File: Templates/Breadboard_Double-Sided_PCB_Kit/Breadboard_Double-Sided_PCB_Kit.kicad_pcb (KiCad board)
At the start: 2 copper layers, 70 x 30 mm, 276 parts

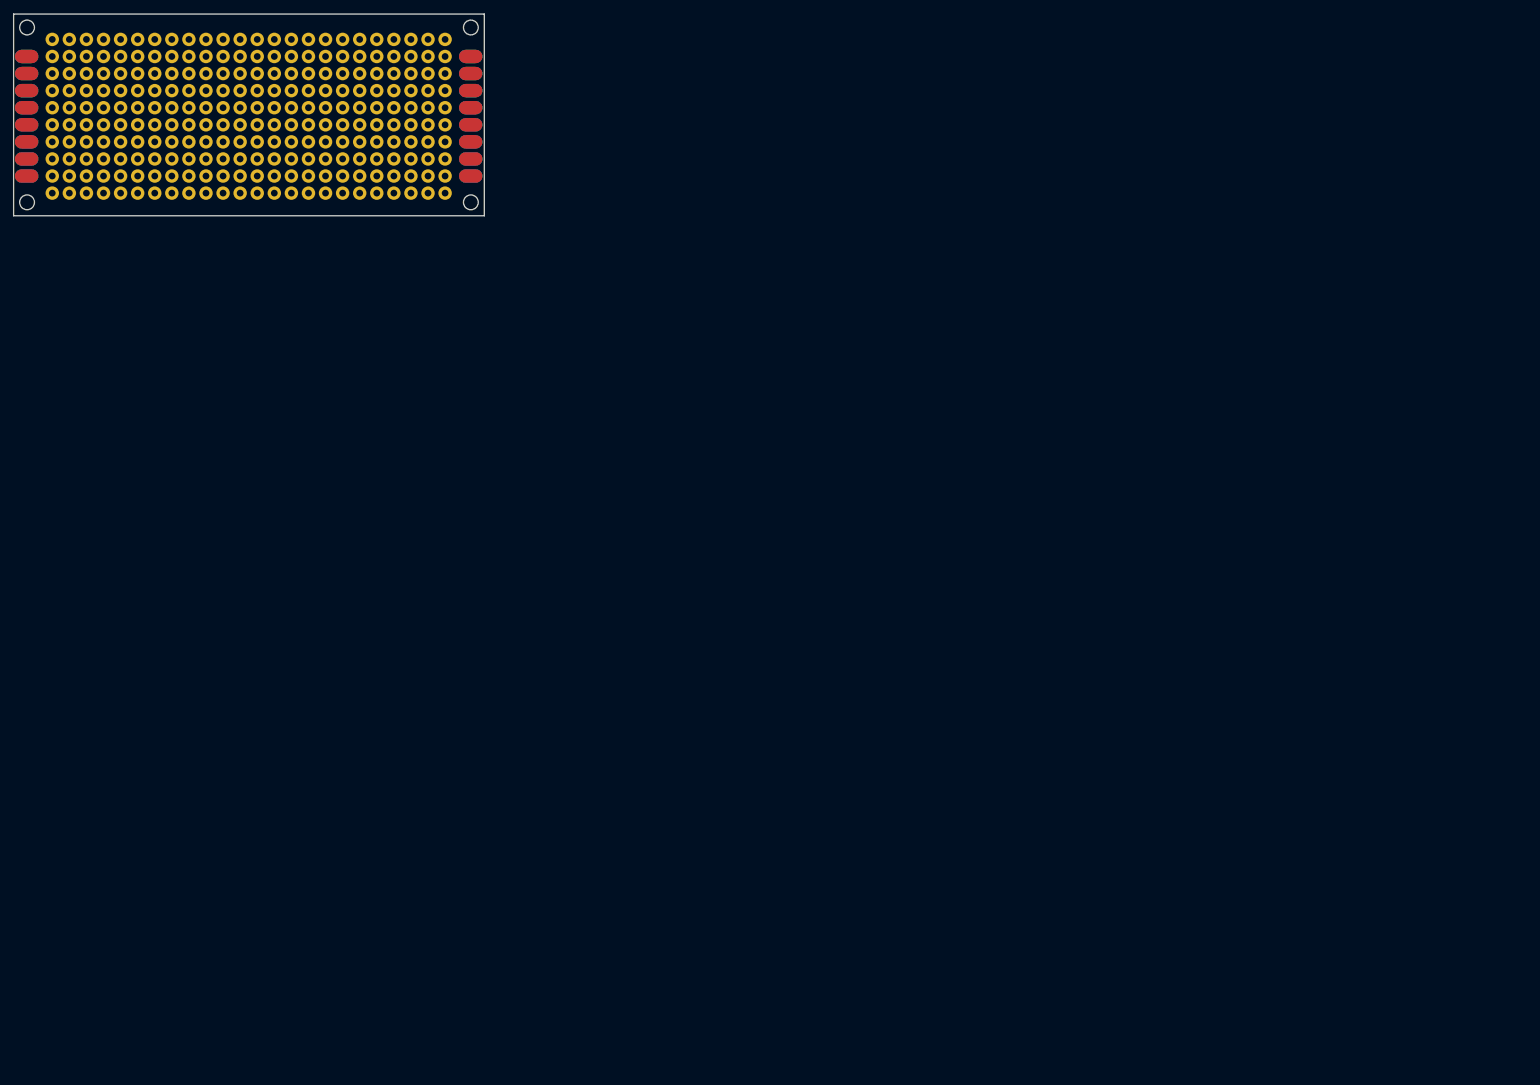
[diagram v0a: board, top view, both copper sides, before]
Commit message: Add all boards in PCB kit.
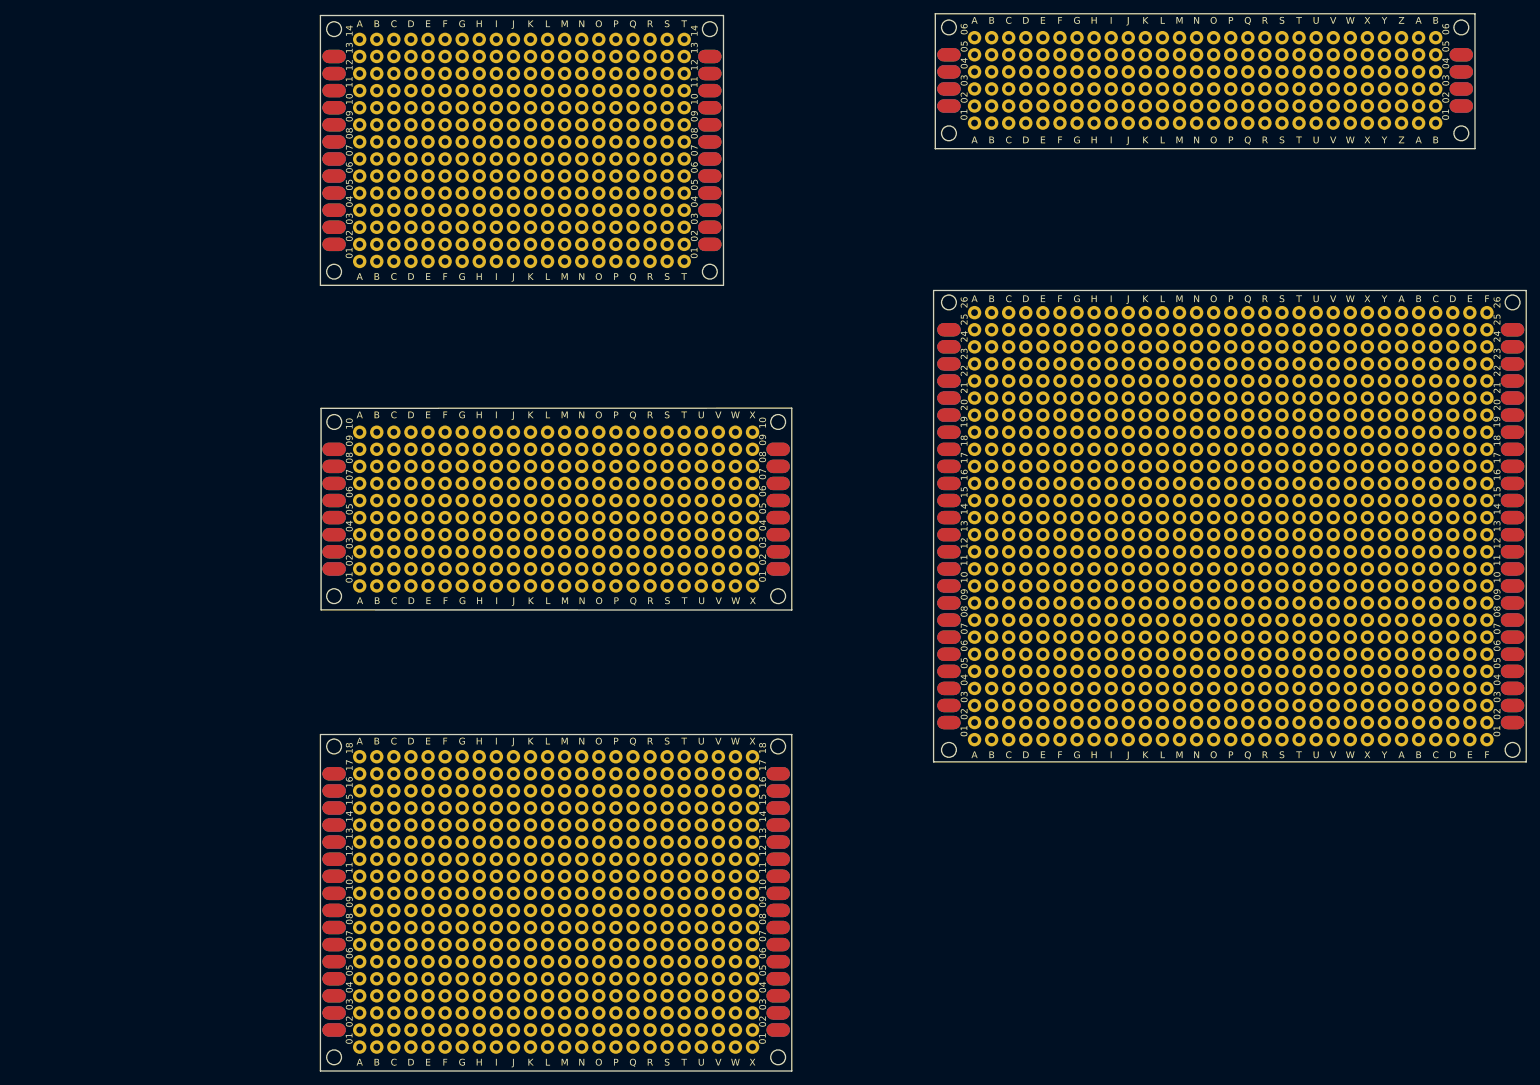
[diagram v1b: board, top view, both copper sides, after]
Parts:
- added REF**: Label, WallLabs:Breadboard_2.54mm_Pad_3.5x2mm, F.Cu at (245.1, 114.3)
- added REF**: Label, WallLabs:Breadboard_2.54mm_Pad_3.5x2mm, B.Cu at (245.1, 116.8)
- added REF**: Label, WallLabs:Breadboard_2.54mm_TH_Pad_2mm, F.Cu at (238.8, 132.1)
- added REF**: Label, WallLabs:Breadboard_2.54mm_TH_Pad_2mm, F.Cu at (104.1, 53.3)
- added REF**: Label, WallLabs:Breadboard_2.54mm_TH_Pad_2mm, F.Cu at (101.6, 53.3)
- added REF**: Label, WallLabs:Breadboard_2.54mm_TH_Pad_2mm, F.Cu at (99.1, 53.3)
- added REF**: Label, WallLabs:Breadboard_2.54mm_TH_Pad_2mm, F.Cu at (96.5, 53.3)
- added REF**: Label, WallLabs:Breadboard_2.54mm_TH_Pad_2mm, F.Cu at (94.0, 53.3)
- added REF**: Label, WallLabs:Breadboard_2.54mm_TH_Pad_2mm, F.Cu at (91.4, 53.3)
- added REF**: Label, WallLabs:Breadboard_2.54mm_TH_Pad_2mm, F.Cu at (88.9, 53.3)
- added REF**: Label, WallLabs:Breadboard_2.54mm_TH_Pad_2mm, F.Cu at (86.4, 53.3)
- added REF**: Label, WallLabs:Breadboard_2.54mm_TH_Pad_2mm, F.Cu at (83.8, 53.3)
- added REF**: Label, WallLabs:Breadboard_2.54mm_TH_Pad_2mm, F.Cu at (81.3, 53.3)
- added REF**: Label, WallLabs:Breadboard_2.54mm_TH_Pad_2mm, F.Cu at (236.2, 132.1)
- added REF**: Label, WallLabs:Breadboard_2.54mm_TH_Pad_2mm, F.Cu at (78.7, 53.3)
- added REF**: Label, WallLabs:Breadboard_2.54mm_TH_Pad_2mm, F.Cu at (76.2, 53.3)
- added REF**: Label, WallLabs:Breadboard_2.54mm_TH_Pad_2mm, F.Cu at (73.7, 53.3)
- added REF**: Label, WallLabs:Breadboard_2.54mm_TH_Pad_2mm, F.Cu at (121.9, 50.8)
- added REF**: Label, WallLabs:Breadboard_2.54mm_TH_Pad_2mm, F.Cu at (119.4, 50.8)
- added REF**: Label, WallLabs:Breadboard_2.54mm_TH_Pad_2mm, F.Cu at (116.8, 50.8)
- added REF**: Label, WallLabs:Breadboard_2.54mm_TH_Pad_2mm, F.Cu at (114.3, 50.8)
- added REF**: Label, WallLabs:Breadboard_2.54mm_TH_Pad_2mm, F.Cu at (111.8, 50.8)
- added REF**: Label, WallLabs:Breadboard_2.54mm_TH_Pad_2mm, F.Cu at (109.2, 50.8)
- added REF**: Label, WallLabs:Breadboard_2.54mm_TH_Pad_2mm, F.Cu at (106.7, 50.8)
- added REF**: Label, WallLabs:Breadboard_2.54mm_TH_Pad_2mm, F.Cu at (233.7, 132.1)
- added REF**: Label, WallLabs:Breadboard_2.54mm_TH_Pad_2mm, F.Cu at (104.1, 50.8)
- added REF**: Label, WallLabs:Breadboard_2.54mm_TH_Pad_2mm, F.Cu at (101.6, 50.8)
- added REF**: Label, WallLabs:Breadboard_2.54mm_TH_Pad_2mm, F.Cu at (99.1, 50.8)
- added REF**: Label, WallLabs:Breadboard_2.54mm_TH_Pad_2mm, F.Cu at (96.5, 50.8)
- added REF**: Label, WallLabs:Breadboard_2.54mm_TH_Pad_2mm, F.Cu at (94.0, 50.8)
- added REF**: Label, WallLabs:Breadboard_2.54mm_TH_Pad_2mm, F.Cu at (91.4, 50.8)
- added REF**: Label, WallLabs:Breadboard_2.54mm_TH_Pad_2mm, F.Cu at (88.9, 50.8)
- added REF**: Label, WallLabs:Breadboard_2.54mm_TH_Pad_2mm, F.Cu at (86.4, 50.8)
- added REF**: Label, WallLabs:Breadboard_2.54mm_TH_Pad_2mm, F.Cu at (83.8, 50.8)
- added REF**: Label, WallLabs:Breadboard_2.54mm_TH_Pad_2mm, F.Cu at (81.3, 50.8)
- added REF**: Label, WallLabs:Breadboard_2.54mm_TH_Pad_2mm, F.Cu at (231.1, 132.1)
- added REF**: Label, WallLabs:Breadboard_2.54mm_TH_Pad_2mm, F.Cu at (78.7, 50.8)
- added REF**: Label, WallLabs:Breadboard_2.54mm_TH_Pad_2mm, F.Cu at (76.2, 50.8)
- added REF**: Label, WallLabs:Breadboard_2.54mm_TH_Pad_2mm, F.Cu at (73.7, 50.8)
- added REF**: Label, WallLabs:Breadboard_2.54mm_TH_Pad_2mm, F.Cu at (121.9, 48.3)
- added REF**: Label, WallLabs:Breadboard_2.54mm_TH_Pad_2mm, F.Cu at (119.4, 48.3)
- added REF**: Label, WallLabs:Breadboard_2.54mm_TH_Pad_2mm, F.Cu at (116.8, 48.3)
- added REF**: Label, WallLabs:Breadboard_2.54mm_TH_Pad_2mm, F.Cu at (114.3, 48.3)
- added REF**: Label, WallLabs:Breadboard_2.54mm_TH_Pad_2mm, F.Cu at (111.8, 48.3)
- added REF**: Label, WallLabs:Breadboard_2.54mm_TH_Pad_2mm, F.Cu at (109.2, 48.3)
- added REF**: Label, WallLabs:Breadboard_2.54mm_TH_Pad_2mm, F.Cu at (106.7, 48.3)
- added REF**: Label, WallLabs:Breadboard_2.54mm_TH_Pad_2mm, F.Cu at (228.6, 132.1)
- added REF**: Label, WallLabs:Breadboard_2.54mm_TH_Pad_2mm, F.Cu at (104.1, 48.3)
- added REF**: Label, WallLabs:Breadboard_2.54mm_TH_Pad_2mm, F.Cu at (101.6, 48.3)
- added REF**: Label, WallLabs:Breadboard_2.54mm_TH_Pad_2mm, F.Cu at (99.1, 48.3)
- added REF**: Label, WallLabs:Breadboard_2.54mm_TH_Pad_2mm, F.Cu at (96.5, 48.3)
- added REF**: Label, WallLabs:Breadboard_2.54mm_TH_Pad_2mm, F.Cu at (94.0, 48.3)
- added REF**: Label, WallLabs:Breadboard_2.54mm_TH_Pad_2mm, F.Cu at (91.4, 48.3)
- added REF**: Label, WallLabs:Breadboard_2.54mm_TH_Pad_2mm, F.Cu at (88.9, 48.3)
- added REF**: Label, WallLabs:Breadboard_2.54mm_TH_Pad_2mm, F.Cu at (86.4, 48.3)
- added REF**: Label, WallLabs:Breadboard_2.54mm_TH_Pad_2mm, F.Cu at (83.8, 48.3)
- added REF**: Label, WallLabs:Breadboard_2.54mm_TH_Pad_2mm, F.Cu at (81.3, 48.3)
- added REF**: Label, WallLabs:Breadboard_2.54mm_TH_Pad_2mm, F.Cu at (226.1, 132.1)
- added REF**: Label, WallLabs:Breadboard_2.54mm_TH_Pad_2mm, F.Cu at (78.7, 48.3)
- added REF**: Label, WallLabs:Breadboard_2.54mm_TH_Pad_2mm, F.Cu at (76.2, 48.3)
- added REF**: Label, WallLabs:Breadboard_2.54mm_TH_Pad_2mm, F.Cu at (73.7, 48.3)
- added REF**: Label, WallLabs:Breadboard_2.54mm_TH_Pad_2mm, F.Cu at (121.9, 45.7)
- added REF**: Label, WallLabs:Breadboard_2.54mm_TH_Pad_2mm, F.Cu at (119.4, 45.7)
- added REF**: Label, WallLabs:Breadboard_2.54mm_TH_Pad_2mm, F.Cu at (116.8, 45.7)
- added REF**: Label, WallLabs:Breadboard_2.54mm_TH_Pad_2mm, F.Cu at (114.3, 45.7)
- added REF**: Label, WallLabs:Breadboard_2.54mm_TH_Pad_2mm, F.Cu at (111.8, 45.7)
- added REF**: Label, WallLabs:Breadboard_2.54mm_TH_Pad_2mm, F.Cu at (109.2, 45.7)
- added REF**: Label, WallLabs:Breadboard_2.54mm_TH_Pad_2mm, F.Cu at (106.7, 45.7)
- added REF**: Label, WallLabs:Breadboard_2.54mm_TH_Pad_2mm, F.Cu at (223.5, 132.1)
- added REF**: Label, WallLabs:Breadboard_2.54mm_TH_Pad_2mm, F.Cu at (104.1, 45.7)
- added REF**: Label, WallLabs:Breadboard_2.54mm_TH_Pad_2mm, F.Cu at (101.6, 45.7)
- added REF**: Label, WallLabs:Breadboard_2.54mm_TH_Pad_2mm, F.Cu at (99.1, 45.7)
- added REF**: Label, WallLabs:Breadboard_2.54mm_TH_Pad_2mm, F.Cu at (96.5, 45.7)
- added REF**: Label, WallLabs:Breadboard_2.54mm_TH_Pad_2mm, F.Cu at (94.0, 45.7)
- added REF**: Label, WallLabs:Breadboard_2.54mm_TH_Pad_2mm, F.Cu at (91.4, 45.7)
- added REF**: Label, WallLabs:Breadboard_2.54mm_TH_Pad_2mm, F.Cu at (88.9, 45.7)
- added REF**: Label, WallLabs:Breadboard_2.54mm_TH_Pad_2mm, F.Cu at (86.4, 45.7)
- added REF**: Label, WallLabs:Breadboard_2.54mm_TH_Pad_2mm, F.Cu at (83.8, 45.7)
- added REF**: Label, WallLabs:Breadboard_2.54mm_TH_Pad_2mm, F.Cu at (81.3, 45.7)
- added REF**: Label, WallLabs:Breadboard_2.54mm_TH_Pad_2mm, F.Cu at (221.0, 132.1)
- added REF**: Label, WallLabs:Breadboard_2.54mm_TH_Pad_2mm, F.Cu at (78.7, 45.7)
- added REF**: Label, WallLabs:Breadboard_2.54mm_TH_Pad_2mm, F.Cu at (76.2, 45.7)
- added REF**: Label, WallLabs:Breadboard_2.54mm_TH_Pad_2mm, F.Cu at (73.7, 45.7)
- added REF**: Label, WallLabs:Breadboard_2.54mm_TH_Pad_2mm, F.Cu at (121.9, 43.2)
- added REF**: Label, WallLabs:Breadboard_2.54mm_TH_Pad_2mm, F.Cu at (119.4, 43.2)
- added REF**: Label, WallLabs:Breadboard_2.54mm_TH_Pad_2mm, F.Cu at (116.8, 43.2)
- added REF**: Label, WallLabs:Breadboard_2.54mm_TH_Pad_2mm, F.Cu at (114.3, 43.2)
- added REF**: Label, WallLabs:Breadboard_2.54mm_TH_Pad_2mm, F.Cu at (111.8, 43.2)
- added REF**: Label, WallLabs:Breadboard_2.54mm_TH_Pad_2mm, F.Cu at (109.2, 43.2)
- added REF**: Label, WallLabs:Breadboard_2.54mm_TH_Pad_2mm, F.Cu at (106.7, 43.2)
- added REF**: Label, WallLabs:Breadboard_2.54mm_TH_Pad_2mm, F.Cu at (218.4, 132.1)
- added REF**: Label, WallLabs:Breadboard_2.54mm_TH_Pad_2mm, F.Cu at (104.1, 43.2)
- added REF**: Label, WallLabs:Breadboard_2.54mm_TH_Pad_2mm, F.Cu at (101.6, 43.2)
- added REF**: Label, WallLabs:Breadboard_2.54mm_TH_Pad_2mm, F.Cu at (99.1, 43.2)
- added REF**: Label, WallLabs:Breadboard_2.54mm_TH_Pad_2mm, F.Cu at (96.5, 43.2)
- added REF**: Label, WallLabs:Breadboard_2.54mm_TH_Pad_2mm, F.Cu at (94.0, 43.2)
- added REF**: Label, WallLabs:Breadboard_2.54mm_TH_Pad_2mm, F.Cu at (91.4, 43.2)
- added REF**: Label, WallLabs:Breadboard_2.54mm_TH_Pad_2mm, F.Cu at (88.9, 43.2)
- added REF**: Label, WallLabs:Breadboard_2.54mm_TH_Pad_2mm, F.Cu at (86.4, 43.2)
- added REF**: Label, WallLabs:Breadboard_2.54mm_TH_Pad_2mm, F.Cu at (83.8, 43.2)
- added REF**: Label, WallLabs:Breadboard_2.54mm_TH_Pad_2mm, F.Cu at (81.3, 43.2)
- added REF**: Label, WallLabs:Breadboard_2.54mm_TH_Pad_2mm, F.Cu at (215.9, 132.1)
- added REF**: Label, WallLabs:Breadboard_2.54mm_TH_Pad_2mm, F.Cu at (78.7, 43.2)
- added REF**: Label, WallLabs:Breadboard_2.54mm_TH_Pad_2mm, F.Cu at (76.2, 43.2)
- added REF**: Label, WallLabs:Breadboard_2.54mm_TH_Pad_2mm, F.Cu at (73.7, 43.2)
- added REF**: Label, WallLabs:Breadboard_2.54mm_TH_Pad_2mm, F.Cu at (121.9, 40.6)
- added REF**: Label, WallLabs:Breadboard_2.54mm_TH_Pad_2mm, F.Cu at (119.4, 40.6)
- added REF**: Label, WallLabs:Breadboard_2.54mm_TH_Pad_2mm, F.Cu at (116.8, 40.6)
- added REF**: Label, WallLabs:Breadboard_2.54mm_TH_Pad_2mm, F.Cu at (114.3, 40.6)
- added REF**: Label, WallLabs:Breadboard_2.54mm_TH_Pad_2mm, F.Cu at (111.8, 40.6)
- added REF**: Label, WallLabs:Breadboard_2.54mm_TH_Pad_2mm, F.Cu at (109.2, 40.6)
- added REF**: Label, WallLabs:Breadboard_2.54mm_TH_Pad_2mm, F.Cu at (106.7, 40.6)
- added REF**: Label, WallLabs:Breadboard_2.54mm_Pad_3.5x2mm, F.Cu at (245.1, 104.1)
- added REF**: Label, WallLabs:Breadboard_2.54mm_TH_Pad_2mm, F.Cu at (213.4, 132.1)
- added REF**: Label, WallLabs:Breadboard_2.54mm_TH_Pad_2mm, F.Cu at (104.1, 40.6)
- added REF**: Label, WallLabs:Breadboard_2.54mm_TH_Pad_2mm, F.Cu at (101.6, 40.6)
- added REF**: Label, WallLabs:Breadboard_2.54mm_TH_Pad_2mm, F.Cu at (99.1, 40.6)
- added REF**: Label, WallLabs:Breadboard_2.54mm_TH_Pad_2mm, F.Cu at (96.5, 40.6)
- added REF**: Label, WallLabs:Breadboard_2.54mm_TH_Pad_2mm, F.Cu at (94.0, 40.6)
- added REF**: Label, WallLabs:Breadboard_2.54mm_TH_Pad_2mm, F.Cu at (91.4, 40.6)
- added REF**: Label, WallLabs:Breadboard_2.54mm_TH_Pad_2mm, F.Cu at (88.9, 40.6)
- added REF**: Label, WallLabs:Breadboard_2.54mm_TH_Pad_2mm, F.Cu at (86.4, 40.6)
- added REF**: Label, WallLabs:Breadboard_2.54mm_TH_Pad_2mm, F.Cu at (83.8, 40.6)
- added REF**: Label, WallLabs:Breadboard_2.54mm_TH_Pad_2mm, F.Cu at (81.3, 40.6)
- added REF**: Label, WallLabs:Breadboard_2.54mm_TH_Pad_2mm, F.Cu at (210.8, 132.1)
- added REF**: Label, WallLabs:Breadboard_2.54mm_TH_Pad_2mm, F.Cu at (78.7, 40.6)
- added REF**: Label, WallLabs:Breadboard_2.54mm_TH_Pad_2mm, F.Cu at (76.2, 40.6)
- added REF**: Label, WallLabs:Breadboard_2.54mm_TH_Pad_2mm, F.Cu at (73.7, 40.6)
- added REF**: Label, WallLabs:Breadboard_2.54mm_TH_Pad_2mm, F.Cu at (121.9, 38.1)
- added REF**: Label, WallLabs:Breadboard_2.54mm_TH_Pad_2mm, F.Cu at (119.4, 38.1)
- added REF**: Label, WallLabs:Breadboard_2.54mm_TH_Pad_2mm, F.Cu at (116.8, 38.1)
- added REF**: Label, WallLabs:Breadboard_2.54mm_TH_Pad_2mm, F.Cu at (114.3, 38.1)
- added REF**: Label, WallLabs:Breadboard_2.54mm_TH_Pad_2mm, F.Cu at (111.8, 38.1)
- added REF**: Label, WallLabs:Breadboard_2.54mm_TH_Pad_2mm, F.Cu at (109.2, 38.1)
- added REF**: Label, WallLabs:Breadboard_2.54mm_TH_Pad_2mm, F.Cu at (106.7, 38.1)
- added REF**: Label, WallLabs:Breadboard_2.54mm_TH_Pad_2mm, F.Cu at (208.3, 132.1)
- added REF**: Label, WallLabs:Breadboard_2.54mm_TH_Pad_2mm, F.Cu at (104.1, 38.1)
- added REF**: Label, WallLabs:Breadboard_2.54mm_TH_Pad_2mm, F.Cu at (101.6, 38.1)
- added REF**: Label, WallLabs:Breadboard_2.54mm_TH_Pad_2mm, F.Cu at (99.1, 38.1)
- added REF**: Label, WallLabs:Breadboard_2.54mm_TH_Pad_2mm, F.Cu at (96.5, 38.1)
- added REF**: Label, WallLabs:Breadboard_2.54mm_TH_Pad_2mm, F.Cu at (94.0, 38.1)
- added REF**: Label, WallLabs:Breadboard_2.54mm_TH_Pad_2mm, F.Cu at (91.4, 38.1)
- added REF**: Label, WallLabs:Breadboard_2.54mm_TH_Pad_2mm, F.Cu at (88.9, 38.1)
- added REF**: Label, WallLabs:Breadboard_2.54mm_TH_Pad_2mm, F.Cu at (86.4, 38.1)
- added REF**: Label, WallLabs:Breadboard_2.54mm_TH_Pad_2mm, F.Cu at (83.8, 38.1)
- added REF**: Label, WallLabs:Breadboard_2.54mm_TH_Pad_2mm, F.Cu at (81.3, 38.1)
- added REF**: Label, WallLabs:Breadboard_2.54mm_TH_Pad_2mm, F.Cu at (205.7, 132.1)
- added REF**: Label, WallLabs:Breadboard_2.54mm_TH_Pad_2mm, F.Cu at (78.7, 38.1)
- added REF**: Label, WallLabs:Breadboard_2.54mm_TH_Pad_2mm, F.Cu at (76.2, 38.1)
- added REF**: Label, WallLabs:Breadboard_2.54mm_TH_Pad_2mm, F.Cu at (73.7, 38.1)
- added REF**: Label, WallLabs:Breadboard_2.54mm_TH_Pad_2mm, F.Cu at (121.9, 35.6)
- added REF**: Label, WallLabs:Breadboard_2.54mm_TH_Pad_2mm, F.Cu at (119.4, 35.6)
- added REF**: Label, WallLabs:Breadboard_2.54mm_TH_Pad_2mm, F.Cu at (116.8, 35.6)
- added REF**: Label, WallLabs:Breadboard_2.54mm_TH_Pad_2mm, F.Cu at (114.3, 35.6)
- added REF**: Label, WallLabs:Breadboard_2.54mm_TH_Pad_2mm, F.Cu at (111.8, 35.6)
- added REF**: Label, WallLabs:Breadboard_2.54mm_TH_Pad_2mm, F.Cu at (109.2, 35.6)
- added REF**: Label, WallLabs:Breadboard_2.54mm_TH_Pad_2mm, F.Cu at (106.7, 35.6)
- added REF**: Label, WallLabs:Breadboard_2.54mm_TH_Pad_2mm, F.Cu at (203.2, 132.1)
- added REF**: Label, WallLabs:Breadboard_2.54mm_TH_Pad_2mm, F.Cu at (104.1, 35.6)
- added REF**: Label, WallLabs:Breadboard_2.54mm_TH_Pad_2mm, F.Cu at (101.6, 35.6)
- added REF**: Label, WallLabs:Breadboard_2.54mm_TH_Pad_2mm, F.Cu at (99.1, 35.6)
- added REF**: Label, WallLabs:Breadboard_2.54mm_TH_Pad_2mm, F.Cu at (96.5, 35.6)
- added REF**: Label, WallLabs:Breadboard_2.54mm_TH_Pad_2mm, F.Cu at (94.0, 35.6)
- added REF**: Label, WallLabs:Breadboard_2.54mm_TH_Pad_2mm, F.Cu at (91.4, 35.6)
- added REF**: Label, WallLabs:Breadboard_2.54mm_TH_Pad_2mm, F.Cu at (88.9, 35.6)
- added REF**: Label, WallLabs:Breadboard_2.54mm_TH_Pad_2mm, F.Cu at (86.4, 35.6)
- added REF**: Label, WallLabs:Breadboard_2.54mm_TH_Pad_2mm, F.Cu at (83.8, 35.6)
- added REF**: Label, WallLabs:Breadboard_2.54mm_TH_Pad_2mm, F.Cu at (81.3, 35.6)
- added REF**: Label, WallLabs:Breadboard_2.54mm_TH_Pad_2mm, F.Cu at (200.7, 132.1)
- added REF**: Label, WallLabs:Breadboard_2.54mm_TH_Pad_2mm, F.Cu at (78.7, 35.6)
- added REF**: Label, WallLabs:Breadboard_2.54mm_TH_Pad_2mm, F.Cu at (76.2, 35.6)
- added REF**: Label, WallLabs:Breadboard_2.54mm_TH_Pad_2mm, F.Cu at (73.7, 35.6)
- added REF**: Label, WallLabs:Breadboard_2.54mm_TH_Pad_2mm, F.Cu at (121.9, 33.0)
- added REF**: Label, WallLabs:Breadboard_2.54mm_TH_Pad_2mm, F.Cu at (119.4, 33.0)
- added REF**: Label, WallLabs:Breadboard_2.54mm_TH_Pad_2mm, F.Cu at (116.8, 33.0)
- added REF**: Label, WallLabs:Breadboard_2.54mm_TH_Pad_2mm, F.Cu at (114.3, 33.0)
- added REF**: Label, WallLabs:Breadboard_2.54mm_TH_Pad_2mm, F.Cu at (111.8, 33.0)
- added REF**: Label, WallLabs:Breadboard_2.54mm_TH_Pad_2mm, F.Cu at (109.2, 33.0)
- added REF**: Label, WallLabs:Breadboard_2.54mm_TH_Pad_2mm, F.Cu at (106.7, 33.0)
- added REF**: Label, WallLabs:Breadboard_2.54mm_TH_Pad_2mm, F.Cu at (198.1, 132.1)
- added REF**: Label, WallLabs:Breadboard_2.54mm_TH_Pad_2mm, F.Cu at (104.1, 33.0)
- added REF**: Label, WallLabs:Breadboard_2.54mm_TH_Pad_2mm, F.Cu at (101.6, 33.0)
- added REF**: Label, WallLabs:Breadboard_2.54mm_TH_Pad_2mm, F.Cu at (99.1, 33.0)
- added REF**: Label, WallLabs:Breadboard_2.54mm_TH_Pad_2mm, F.Cu at (96.5, 33.0)
- added REF**: Label, WallLabs:Breadboard_2.54mm_TH_Pad_2mm, F.Cu at (94.0, 33.0)
- added REF**: Label, WallLabs:Breadboard_2.54mm_TH_Pad_2mm, F.Cu at (91.4, 33.0)
- added REF**: Label, WallLabs:Breadboard_2.54mm_TH_Pad_2mm, F.Cu at (88.9, 33.0)
- added REF**: Label, WallLabs:Breadboard_2.54mm_TH_Pad_2mm, F.Cu at (86.4, 33.0)
- added REF**: Label, WallLabs:Breadboard_2.54mm_TH_Pad_2mm, F.Cu at (83.8, 33.0)
- added REF**: Label, WallLabs:Breadboard_2.54mm_TH_Pad_2mm, F.Cu at (81.3, 33.0)
- added REF**: Label, WallLabs:Breadboard_2.54mm_TH_Pad_2mm, F.Cu at (195.6, 132.1)
- added REF**: Label, WallLabs:Breadboard_2.54mm_TH_Pad_2mm, F.Cu at (78.7, 33.0)
- added REF**: Label, WallLabs:Breadboard_2.54mm_TH_Pad_2mm, F.Cu at (76.2, 33.0)
- added REF**: Label, WallLabs:Breadboard_2.54mm_TH_Pad_2mm, F.Cu at (73.7, 33.0)
- added REF**: Label, WallLabs:Breadboard_2.54mm_TH_Pad_2mm, F.Cu at (121.9, 30.5)
- added REF**: Label, WallLabs:Breadboard_2.54mm_TH_Pad_2mm, F.Cu at (119.4, 30.5)
- added REF**: Label, WallLabs:Breadboard_2.54mm_TH_Pad_2mm, F.Cu at (116.8, 30.5)
- added REF**: Label, WallLabs:Breadboard_2.54mm_TH_Pad_2mm, F.Cu at (114.3, 30.5)
- added REF**: Label, WallLabs:Breadboard_2.54mm_TH_Pad_2mm, F.Cu at (111.8, 30.5)
- added REF**: Label, WallLabs:Breadboard_2.54mm_TH_Pad_2mm, F.Cu at (109.2, 30.5)
- added REF**: Label, WallLabs:Breadboard_2.54mm_TH_Pad_2mm, F.Cu at (106.7, 30.5)
- added REF**: Label, WallLabs:Breadboard_2.54mm_TH_Pad_2mm, F.Cu at (193.0, 132.1)
- added REF**: Label, WallLabs:Breadboard_2.54mm_TH_Pad_2mm, F.Cu at (104.1, 30.5)
- added REF**: Label, WallLabs:Breadboard_2.54mm_TH_Pad_2mm, F.Cu at (101.6, 30.5)
- added REF**: Label, WallLabs:Breadboard_2.54mm_TH_Pad_2mm, F.Cu at (99.1, 30.5)
- added REF**: Label, WallLabs:Breadboard_2.54mm_TH_Pad_2mm, F.Cu at (96.5, 30.5)
- added REF**: Label, WallLabs:Breadboard_2.54mm_TH_Pad_2mm, F.Cu at (94.0, 30.5)
- added REF**: Label, WallLabs:Breadboard_2.54mm_TH_Pad_2mm, F.Cu at (91.4, 30.5)
- added REF**: Label, WallLabs:Breadboard_2.54mm_TH_Pad_2mm, F.Cu at (88.9, 30.5)
- added REF**: Label, WallLabs:Breadboard_2.54mm_TH_Pad_2mm, F.Cu at (86.4, 30.5)
- added REF**: Label, WallLabs:Breadboard_2.54mm_TH_Pad_2mm, F.Cu at (83.8, 30.5)
- added REF**: Label, WallLabs:Breadboard_2.54mm_TH_Pad_2mm, F.Cu at (81.3, 30.5)
- added REF**: Label, WallLabs:Breadboard_2.54mm_TH_Pad_2mm, F.Cu at (190.5, 132.1)
- added REF**: Label, WallLabs:Breadboard_2.54mm_TH_Pad_2mm, F.Cu at (78.7, 30.5)
- added REF**: Label, WallLabs:Breadboard_2.54mm_TH_Pad_2mm, F.Cu at (76.2, 30.5)
- added REF**: Label, WallLabs:Breadboard_2.54mm_TH_Pad_2mm, F.Cu at (73.7, 30.5)
- added REF**: Label, WallLabs:Breadboard_2.54mm_TH_Pad_2mm, F.Cu at (121.9, 27.9)
- added REF**: Label, WallLabs:Breadboard_2.54mm_TH_Pad_2mm, F.Cu at (119.4, 27.9)
- added REF**: Label, WallLabs:Breadboard_2.54mm_TH_Pad_2mm, F.Cu at (116.8, 27.9)
- added REF**: Label, WallLabs:Breadboard_2.54mm_TH_Pad_2mm, F.Cu at (114.3, 27.9)
- added REF**: Label, WallLabs:Breadboard_2.54mm_TH_Pad_2mm, F.Cu at (111.8, 27.9)
- added REF**: Label, WallLabs:Breadboard_2.54mm_TH_Pad_2mm, F.Cu at (109.2, 27.9)
- added REF**: Label, WallLabs:Breadboard_2.54mm_TH_Pad_2mm, F.Cu at (106.7, 27.9)
- added REF**: Label, WallLabs:Breadboard_2.54mm_Pad_3.5x2mm, F.Cu at (245.1, 99.1)
- added REF**: Label, WallLabs:Breadboard_2.54mm_TH_Pad_2mm, F.Cu at (188.0, 132.1)
- added REF**: Label, WallLabs:Breadboard_2.54mm_TH_Pad_2mm, F.Cu at (104.1, 27.9)
- added REF**: Label, WallLabs:Breadboard_2.54mm_TH_Pad_2mm, F.Cu at (101.6, 27.9)
- added REF**: Label, WallLabs:Breadboard_2.54mm_TH_Pad_2mm, F.Cu at (99.1, 27.9)
- added REF**: Label, WallLabs:Breadboard_2.54mm_TH_Pad_2mm, F.Cu at (96.5, 27.9)
- added REF**: Label, WallLabs:Breadboard_2.54mm_TH_Pad_2mm, F.Cu at (94.0, 27.9)
- added REF**: Label, WallLabs:Breadboard_2.54mm_TH_Pad_2mm, F.Cu at (91.4, 27.9)
- added REF**: Label, WallLabs:Breadboard_2.54mm_TH_Pad_2mm, F.Cu at (88.9, 27.9)
- added REF**: Label, WallLabs:Breadboard_2.54mm_TH_Pad_2mm, F.Cu at (86.4, 27.9)
- added REF**: Label, WallLabs:Breadboard_2.54mm_TH_Pad_2mm, F.Cu at (83.8, 27.9)
- added REF**: Label, WallLabs:Breadboard_2.54mm_TH_Pad_2mm, F.Cu at (81.3, 27.9)
- added REF**: Label, WallLabs:Breadboard_2.54mm_TH_Pad_2mm, F.Cu at (185.4, 132.1)
- added REF**: Label, WallLabs:Breadboard_2.54mm_TH_Pad_2mm, F.Cu at (78.7, 27.9)
- added REF**: Label, WallLabs:Breadboard_2.54mm_TH_Pad_2mm, F.Cu at (76.2, 27.9)
- added REF**: Label, WallLabs:Breadboard_2.54mm_Pad_3.5x2mm, B.Cu at (69.8, 30.5)
- added REF**: Label, WallLabs:Breadboard_2.54mm_TH_Pad_2mm, F.Cu at (73.7, 27.9)
- added REF**: Label, WallLabs:Breadboard_2.54mm_Pad_3.5x2mm, F.Cu at (69.8, 30.5)
- added REF**: Label, WallLabs:Breadboard_2.54mm_Pad_3.5x2mm, F.Cu at (69.8, 58.4)
- added REF**: Label, WallLabs:Breadboard_2.54mm_Pad_3.5x2mm, B.Cu at (69.8, 58.4)
- added REF**: MountingHole_2.2mm_M2_ISO14580, MountingHole:MountingHole_2.2mm_M2_ISO14580, F.Cu at (69.8, 62.5)
- added REF**: Label, WallLabs:Breadboard_2.54mm_Pad_3.5x2mm, F.Cu at (69.8, 53.3)
- added REF**: Label, WallLabs:Breadboard_2.54mm_Pad_3.5x2mm, F.Cu at (69.8, 55.9)
- added REF**: Label, WallLabs:Breadboard_2.54mm_TH_Pad_2mm, F.Cu at (182.9, 132.1)
- added REF**: Label, WallLabs:Breadboard_2.54mm_Pad_3.5x2mm, B.Cu at (69.8, 55.9)
- added REF**: Label, WallLabs:Breadboard_2.54mm_Pad_3.5x2mm, B.Cu at (69.8, 53.3)
- added REF**: Label, WallLabs:Breadboard_2.54mm_Pad_3.5x2mm, F.Cu at (69.8, 50.8)
- added REF**: Label, WallLabs:Breadboard_2.54mm_Pad_3.5x2mm, B.Cu at (69.8, 50.8)
- added REF**: Label, WallLabs:Breadboard_2.54mm_Pad_3.5x2mm, F.Cu at (69.8, 48.3)
- added REF**: Label, WallLabs:Breadboard_2.54mm_Pad_3.5x2mm, B.Cu at (69.8, 35.6)
- added REF**: Label, WallLabs:Breadboard_2.54mm_Pad_3.5x2mm, F.Cu at (69.8, 43.2)
- added REF**: Label, WallLabs:Breadboard_2.54mm_Pad_3.5x2mm, B.Cu at (69.8, 38.1)
- added REF**: Label, WallLabs:Breadboard_2.54mm_Pad_3.5x2mm, F.Cu at (69.8, 45.7)
- added REF**: Label, WallLabs:Breadboard_2.54mm_Pad_3.5x2mm, B.Cu at (69.8, 40.6)
- added REF**: Label, WallLabs:Breadboard_2.54mm_TH_Pad_2mm, F.Cu at (180.3, 132.1)
- added REF**: Label, WallLabs:Breadboard_2.54mm_Pad_3.5x2mm, F.Cu at (69.8, 35.6)
- added REF**: Label, WallLabs:Breadboard_2.54mm_Pad_3.5x2mm, B.Cu at (69.8, 43.2)
- added REF**: Label, WallLabs:Breadboard_2.54mm_Pad_3.5x2mm, B.Cu at (69.8, 48.3)
- added REF**: Label, WallLabs:Breadboard_2.54mm_Pad_3.5x2mm, B.Cu at (69.8, 33.0)
- added REF**: Label, WallLabs:Breadboard_2.54mm_Pad_3.5x2mm, F.Cu at (69.8, 38.1)
- added REF**: Label, WallLabs:Breadboard_2.54mm_Pad_3.5x2mm, F.Cu at (69.8, 33.0)
- added REF**: Label, WallLabs:Breadboard_2.54mm_Pad_3.5x2mm, B.Cu at (69.8, 45.7)
- added REF**: Label, WallLabs:Breadboard_2.54mm_Pad_3.5x2mm, F.Cu at (69.8, 40.6)
- added REF**: MountingHole_2.2mm_M2_ISO14580, MountingHole:MountingHole_2.2mm_M2_ISO14580, F.Cu at (69.8, 26.4)
- added REF**: Label, WallLabs:Breadboard_2.54mm_Pad_3.5x2mm, B.Cu at (135.9, 165.1)
- added REF**: Label, WallLabs:Breadboard_2.54mm_TH_Pad_2mm, F.Cu at (177.8, 132.1)
- added REF**: Label, WallLabs:Breadboard_2.54mm_Pad_3.5x2mm, B.Cu at (135.9, 157.5)
- added REF**: Label, WallLabs:Breadboard_2.54mm_Pad_3.5x2mm, B.Cu at (135.9, 167.6)
- added REF**: Label, WallLabs:Breadboard_2.54mm_Pad_3.5x2mm, B.Cu at (135.9, 154.9)
- added REF**: Label, WallLabs:Breadboard_2.54mm_Pad_3.5x2mm, B.Cu at (135.9, 160.0)
- added REF**: Label, WallLabs:Breadboard_2.54mm_Pad_3.5x2mm, B.Cu at (135.9, 152.4)
- added REF**: Label, WallLabs:Breadboard_2.54mm_Pad_3.5x2mm, B.Cu at (135.9, 170.2)
- added REF**: Label, WallLabs:Breadboard_2.54mm_Pad_3.5x2mm, B.Cu at (135.9, 175.3)
- added REF**: Label, WallLabs:Breadboard_2.54mm_Pad_3.5x2mm, B.Cu at (135.9, 142.2)
- added REF**: Label, WallLabs:Breadboard_2.54mm_Pad_3.5x2mm, B.Cu at (135.9, 147.3)
- added REF**: Label, WallLabs:Breadboard_2.54mm_Pad_3.5x2mm, B.Cu at (135.9, 162.6)
- added REF**: Label, WallLabs:Breadboard_2.54mm_TH_Pad_2mm, F.Cu at (175.3, 132.1)
- added REF**: Label, WallLabs:Breadboard_2.54mm_Pad_3.5x2mm, B.Cu at (135.9, 144.8)
- added REF**: Label, WallLabs:Breadboard_2.54mm_Pad_3.5x2mm, B.Cu at (135.9, 139.7)
- added REF**: Label, WallLabs:Breadboard_2.54mm_Pad_3.5x2mm, B.Cu at (135.9, 172.7)
- added REF**: Label, WallLabs:Breadboard_2.54mm_Pad_3.5x2mm, B.Cu at (135.9, 149.9)
- added REF**: Label, WallLabs:Breadboard_2.54mm_Pad_3.5x2mm, B.Cu at (135.9, 137.2)
- added REF**: Label, WallLabs:Breadboard_2.54mm_Pad_3.5x2mm, B.Cu at (69.8, 149.9)
- added REF**: Label, WallLabs:Breadboard_2.54mm_Pad_3.5x2mm, B.Cu at (69.8, 152.4)
- added REF**: Label, WallLabs:Breadboard_2.54mm_Pad_3.5x2mm, B.Cu at (69.8, 139.7)
- added REF**: Label, WallLabs:Breadboard_2.54mm_Pad_3.5x2mm, B.Cu at (69.8, 144.8)
- added REF**: Label, WallLabs:Breadboard_2.54mm_Pad_3.5x2mm, B.Cu at (69.8, 147.3)
- added REF**: Label, WallLabs:Breadboard_2.54mm_TH_Pad_2mm, F.Cu at (172.7, 132.1)
- added REF**: Label, WallLabs:Breadboard_2.54mm_Pad_3.5x2mm, B.Cu at (69.8, 142.2)
- added REF**: Label, WallLabs:Breadboard_2.54mm_Pad_3.5x2mm, B.Cu at (69.8, 137.2)
- added REF**: Label, WallLabs:Breadboard_2.54mm_Pad_3.5x2mm, B.Cu at (69.8, 160.0)
- added REF**: Label, WallLabs:Breadboard_2.54mm_Pad_3.5x2mm, B.Cu at (69.8, 154.9)
- added REF**: Label, WallLabs:Breadboard_2.54mm_Pad_3.5x2mm, B.Cu at (69.8, 157.5)
- added REF**: Label, WallLabs:Breadboard_2.54mm_Pad_3.5x2mm, B.Cu at (69.8, 167.6)
- added REF**: Label, WallLabs:Breadboard_2.54mm_Pad_3.5x2mm, B.Cu at (69.8, 170.2)
- added REF**: Label, WallLabs:Breadboard_2.54mm_Pad_3.5x2mm, B.Cu at (69.8, 162.6)
- added REF**: Label, WallLabs:Breadboard_2.54mm_Pad_3.5x2mm, B.Cu at (69.8, 165.1)
- added REF**: Label, WallLabs:Breadboard_2.54mm_Pad_3.5x2mm, B.Cu at (69.8, 172.7)
- added REF**: Label, WallLabs:Breadboard_2.54mm_TH_Pad_2mm, F.Cu at (170.2, 132.1)
- added REF**: Label, WallLabs:Breadboard_2.54mm_Pad_3.5x2mm, B.Cu at (69.8, 175.3)
- added REF**: Label, WallLabs:Breadboard_2.54mm_Pad_3.5x2mm, F.Cu at (135.9, 162.6)
- added REF**: Label, WallLabs:Breadboard_2.54mm_Pad_3.5x2mm, F.Cu at (135.9, 160.0)
- added REF**: Label, WallLabs:Breadboard_2.54mm_Pad_3.5x2mm, F.Cu at (135.9, 172.7)
- added REF**: Label, WallLabs:Breadboard_2.54mm_Pad_3.5x2mm, F.Cu at (135.9, 167.6)
- added REF**: Label, WallLabs:Breadboard_2.54mm_Pad_3.5x2mm, F.Cu at (135.9, 165.1)
- added REF**: Label, WallLabs:Breadboard_2.54mm_Pad_3.5x2mm, F.Cu at (135.9, 170.2)
- added REF**: Label, WallLabs:Breadboard_2.54mm_Pad_3.5x2mm, F.Cu at (135.9, 175.3)
- added REF**: Label, WallLabs:Breadboard_2.54mm_Pad_3.5x2mm, F.Cu at (135.9, 152.4)
- added REF**: Label, WallLabs:Breadboard_2.54mm_Pad_3.5x2mm, F.Cu at (135.9, 157.5)
- added REF**: Label, WallLabs:Breadboard_2.54mm_TH_Pad_2mm, F.Cu at (167.6, 132.1)
- added REF**: Label, WallLabs:Breadboard_2.54mm_Pad_3.5x2mm, F.Cu at (135.9, 154.9)
- added REF**: Label, WallLabs:Breadboard_2.54mm_Pad_3.5x2mm, F.Cu at (135.9, 144.8)
- added REF**: Label, WallLabs:Breadboard_2.54mm_Pad_3.5x2mm, F.Cu at (135.9, 142.2)
- added REF**: Label, WallLabs:Breadboard_2.54mm_Pad_3.5x2mm, F.Cu at (135.9, 149.9)
- added REF**: Label, WallLabs:Breadboard_2.54mm_Pad_3.5x2mm, F.Cu at (135.9, 147.3)
- added REF**: Label, WallLabs:Breadboard_2.54mm_Pad_3.5x2mm, F.Cu at (135.9, 139.7)
- added REF**: Label, WallLabs:Breadboard_2.54mm_Pad_3.5x2mm, F.Cu at (135.9, 137.2)
- added REF**: Label, WallLabs:Breadboard_2.54mm_Pad_3.5x2mm, F.Cu at (69.8, 175.3)
- added REF**: Label, WallLabs:Breadboard_2.54mm_Pad_3.5x2mm, F.Cu at (69.8, 172.7)
- added REF**: Label, WallLabs:Breadboard_2.54mm_Pad_3.5x2mm, F.Cu at (69.8, 170.2)
- added REF**: Label, WallLabs:Breadboard_2.54mm_TH_Pad_2mm, F.Cu at (165.1, 132.1)
- added REF**: Label, WallLabs:Breadboard_2.54mm_Pad_3.5x2mm, F.Cu at (69.8, 167.6)
- added REF**: Label, WallLabs:Breadboard_2.54mm_Pad_3.5x2mm, F.Cu at (69.8, 165.1)
- added REF**: Label, WallLabs:Breadboard_2.54mm_Pad_3.5x2mm, F.Cu at (69.8, 162.6)
- added REF**: Label, WallLabs:Breadboard_2.54mm_Pad_3.5x2mm, F.Cu at (69.8, 160.0)
- added REF**: Label, WallLabs:Breadboard_2.54mm_Pad_3.5x2mm, F.Cu at (69.8, 157.5)
- added REF**: Label, WallLabs:Breadboard_2.54mm_Pad_3.5x2mm, F.Cu at (69.8, 154.9)
- added REF**: Label, WallLabs:Breadboard_2.54mm_Pad_3.5x2mm, F.Cu at (69.8, 152.4)
- added REF**: Label, WallLabs:Breadboard_2.54mm_Pad_3.5x2mm, F.Cu at (69.8, 149.9)
- added REF**: Label, WallLabs:Breadboard_2.54mm_Pad_3.5x2mm, F.Cu at (69.8, 147.3)
- added REF**: Label, WallLabs:Breadboard_2.54mm_Pad_3.5x2mm, F.Cu at (69.8, 144.8)
- added REF**: Label, WallLabs:Breadboard_2.54mm_Pad_3.5x2mm, B.Cu at (245.1, 119.4)
- added REF**: Label, WallLabs:Breadboard_2.54mm_TH_Pad_2mm, F.Cu at (241.3, 129.5)
- added REF**: Label, WallLabs:Breadboard_2.54mm_Pad_3.5x2mm, F.Cu at (69.8, 142.2)
- added REF**: Label, WallLabs:Breadboard_2.54mm_Pad_3.5x2mm, F.Cu at (69.8, 139.7)
- added REF**: Label, WallLabs:Breadboard_2.54mm_Pad_3.5x2mm, F.Cu at (69.8, 137.2)
- added REF**: MountingHole_2.2mm_M2_ISO14580, MountingHole:MountingHole_2.2mm_M2_ISO14580, F.Cu at (135.9, 133.1)
- added REF**: MountingHole_2.2mm_M2_ISO14580, MountingHole:MountingHole_2.2mm_M2_ISO14580, F.Cu at (135.9, 179.3)
- added REF**: MountingHole_2.2mm_M2_ISO14580, MountingHole:MountingHole_2.2mm_M2_ISO14580, F.Cu at (69.8, 179.3)
- added REF**: MountingHole_2.2mm_M2_ISO14580, MountingHole:MountingHole_2.2mm_M2_ISO14580, F.Cu at (69.8, 133.1)
- added REF**: VAL**, WallLabs:Breadboard_2.54mm_TH_Pad_2mm, F.Cu at (132.1, 177.8)
- added REF**: VAL**, WallLabs:Breadboard_2.54mm_TH_Pad_2mm, F.Cu at (129.5, 177.8)
- added REF**: VAL**, WallLabs:Breadboard_2.54mm_TH_Pad_2mm, F.Cu at (127.0, 177.8)
- added REF**: Label, WallLabs:Breadboard_2.54mm_TH_Pad_2mm, F.Cu at (238.8, 129.5)
- added REF**: VAL**, WallLabs:Breadboard_2.54mm_TH_Pad_2mm, F.Cu at (124.5, 177.8)
- added REF**: VAL**, WallLabs:Breadboard_2.54mm_TH_Pad_2mm, F.Cu at (121.9, 177.8)
- added REF**: VAL**, WallLabs:Breadboard_2.54mm_TH_Pad_2mm, F.Cu at (119.4, 177.8)
- added REF**: VAL**, WallLabs:Breadboard_2.54mm_TH_Pad_2mm, F.Cu at (116.8, 177.8)
- added REF**: VAL**, WallLabs:Breadboard_2.54mm_TH_Pad_2mm, F.Cu at (114.3, 177.8)
- added REF**: VAL**, WallLabs:Breadboard_2.54mm_TH_Pad_2mm, F.Cu at (111.8, 177.8)
- added REF**: VAL**, WallLabs:Breadboard_2.54mm_TH_Pad_2mm, F.Cu at (109.2, 177.8)
- added REF**: VAL**, WallLabs:Breadboard_2.54mm_TH_Pad_2mm, F.Cu at (106.7, 177.8)
- added REF**: VAL**, WallLabs:Breadboard_2.54mm_TH_Pad_2mm, F.Cu at (104.1, 177.8)
- added REF**: VAL**, WallLabs:Breadboard_2.54mm_TH_Pad_2mm, F.Cu at (101.6, 177.8)
- added REF**: Label, WallLabs:Breadboard_2.54mm_TH_Pad_2mm, F.Cu at (236.2, 129.5)
- added REF**: VAL**, WallLabs:Breadboard_2.54mm_TH_Pad_2mm, F.Cu at (99.1, 177.8)
- added REF**: VAL**, WallLabs:Breadboard_2.54mm_TH_Pad_2mm, F.Cu at (96.5, 177.8)
- added REF**: VAL**, WallLabs:Breadboard_2.54mm_TH_Pad_2mm, F.Cu at (94.0, 177.8)
- added REF**: VAL**, WallLabs:Breadboard_2.54mm_TH_Pad_2mm, F.Cu at (91.4, 177.8)
- added REF**: VAL**, WallLabs:Breadboard_2.54mm_TH_Pad_2mm, F.Cu at (88.9, 177.8)
- added REF**: VAL**, WallLabs:Breadboard_2.54mm_TH_Pad_2mm, F.Cu at (86.4, 177.8)
- added REF**: VAL**, WallLabs:Breadboard_2.54mm_TH_Pad_2mm, F.Cu at (83.8, 177.8)
- added REF**: VAL**, WallLabs:Breadboard_2.54mm_TH_Pad_2mm, F.Cu at (81.3, 177.8)
- added REF**: VAL**, WallLabs:Breadboard_2.54mm_TH_Pad_2mm, F.Cu at (78.7, 177.8)
- added REF**: VAL**, WallLabs:Breadboard_2.54mm_TH_Pad_2mm, F.Cu at (76.2, 177.8)
- added REF**: Label, WallLabs:Breadboard_2.54mm_TH_Pad_2mm, F.Cu at (233.7, 129.5)
- added REF**: VAL**, WallLabs:Breadboard_2.54mm_TH_Pad_2mm, F.Cu at (73.7, 177.8)
- added REF**: VAL**, WallLabs:Breadboard_2.54mm_TH_Pad_2mm, F.Cu at (132.1, 175.3)
- added REF**: VAL**, WallLabs:Breadboard_2.54mm_TH_Pad_2mm, F.Cu at (129.5, 175.3)
- added REF**: VAL**, WallLabs:Breadboard_2.54mm_TH_Pad_2mm, F.Cu at (127.0, 175.3)
- added REF**: VAL**, WallLabs:Breadboard_2.54mm_TH_Pad_2mm, F.Cu at (124.5, 175.3)
- added REF**: VAL**, WallLabs:Breadboard_2.54mm_TH_Pad_2mm, F.Cu at (121.9, 175.3)
- added REF**: VAL**, WallLabs:Breadboard_2.54mm_TH_Pad_2mm, F.Cu at (119.4, 175.3)
- added REF**: VAL**, WallLabs:Breadboard_2.54mm_TH_Pad_2mm, F.Cu at (116.8, 175.3)
- added REF**: VAL**, WallLabs:Breadboard_2.54mm_TH_Pad_2mm, F.Cu at (114.3, 175.3)
- added REF**: VAL**, WallLabs:Breadboard_2.54mm_TH_Pad_2mm, F.Cu at (111.8, 175.3)
- added REF**: Label, WallLabs:Breadboard_2.54mm_TH_Pad_2mm, F.Cu at (231.1, 129.5)
- added REF**: VAL**, WallLabs:Breadboard_2.54mm_TH_Pad_2mm, F.Cu at (109.2, 175.3)
- added REF**: VAL**, WallLabs:Breadboard_2.54mm_TH_Pad_2mm, F.Cu at (106.7, 175.3)
- added REF**: VAL**, WallLabs:Breadboard_2.54mm_TH_Pad_2mm, F.Cu at (104.1, 175.3)
- added REF**: VAL**, WallLabs:Breadboard_2.54mm_TH_Pad_2mm, F.Cu at (101.6, 175.3)
- added REF**: VAL**, WallLabs:Breadboard_2.54mm_TH_Pad_2mm, F.Cu at (99.1, 175.3)
- added REF**: VAL**, WallLabs:Breadboard_2.54mm_TH_Pad_2mm, F.Cu at (96.5, 175.3)
- added REF**: VAL**, WallLabs:Breadboard_2.54mm_TH_Pad_2mm, F.Cu at (94.0, 175.3)
- added REF**: VAL**, WallLabs:Breadboard_2.54mm_TH_Pad_2mm, F.Cu at (91.4, 175.3)
- added REF**: VAL**, WallLabs:Breadboard_2.54mm_TH_Pad_2mm, F.Cu at (88.9, 175.3)
- added REF**: VAL**, WallLabs:Breadboard_2.54mm_TH_Pad_2mm, F.Cu at (86.4, 175.3)
- added REF**: Label, WallLabs:Breadboard_2.54mm_TH_Pad_2mm, F.Cu at (228.6, 129.5)
- added REF**: VAL**, WallLabs:Breadboard_2.54mm_TH_Pad_2mm, F.Cu at (83.8, 175.3)
- added REF**: VAL**, WallLabs:Breadboard_2.54mm_TH_Pad_2mm, F.Cu at (81.3, 175.3)
- added REF**: VAL**, WallLabs:Breadboard_2.54mm_TH_Pad_2mm, F.Cu at (78.7, 175.3)
- added REF**: VAL**, WallLabs:Breadboard_2.54mm_TH_Pad_2mm, F.Cu at (76.2, 175.3)
- added REF**: VAL**, WallLabs:Breadboard_2.54mm_TH_Pad_2mm, F.Cu at (73.7, 175.3)
- added REF**: VAL**, WallLabs:Breadboard_2.54mm_TH_Pad_2mm, F.Cu at (132.1, 172.7)
- added REF**: VAL**, WallLabs:Breadboard_2.54mm_TH_Pad_2mm, F.Cu at (129.5, 172.7)
- added REF**: VAL**, WallLabs:Breadboard_2.54mm_TH_Pad_2mm, F.Cu at (127.0, 172.7)
- added REF**: VAL**, WallLabs:Breadboard_2.54mm_TH_Pad_2mm, F.Cu at (124.5, 172.7)
- added REF**: VAL**, WallLabs:Breadboard_2.54mm_TH_Pad_2mm, F.Cu at (121.9, 172.7)
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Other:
- board size 70 x 30 mm -> 179.3 x 157.2 mm
- net class Default: clearance 0.2 -> 0.25; trace_width 0.25 -> 1; via_dia 0.8 -> 2; via_drill 0.4 -> 1
- rule trace_clearance: 0.2 -> 0.25
- board text added: "01"
- board text added: "02"
- board text added: "03"
- board text added: "04"
- board text added: "05"
- board text added: "06"
- board text added: "07"
- board text added: "08"
- board text added: "09"
- board text added: "10"
- board text added: "11"
- board text added: "12"
- board text added: "13"
- board text added: "14"
- board text added: "15"
- board text added: "16"
- board text added: "17"
- board text added: "18"
- board text added: "19"
- board text added: "20"
- board text added: "21"
- board text added: "22"
- board text added: "23"
- board text added: "24"
- board text added: "25"
- board text added: "26"
- board text added: "A"
- board text added: "B"
- board text added: "C"
- board text added: "D"
- board text added: "E"
- board text added: "F"
- board text added: "G"
- board text added: "H"
- board text added: "I"
- board text added: "J"
- board text added: "K"
- board text added: "L"
- board text added: "M"
- board text added: "N"
- board text added: "O"
- board text added: "P"
- board text added: "Q"
- board text added: "R"
- board text added: "S"
- board text added: "T"
- board text added: "U"
- board text added: "V"
- board text added: "W"
- board text added: "X"
- board text added: "Y"
- board text added: "Z"
